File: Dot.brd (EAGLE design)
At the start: 25.4 x 31.5 mm, 42 parts, among them IC1 CAT24M010TS, IC2 SI1145, U1 ATMEGA328P-MU-QFN32, U2 TMP102, U3 ISL29125, U4 9DoF IMU, U5 BMP18

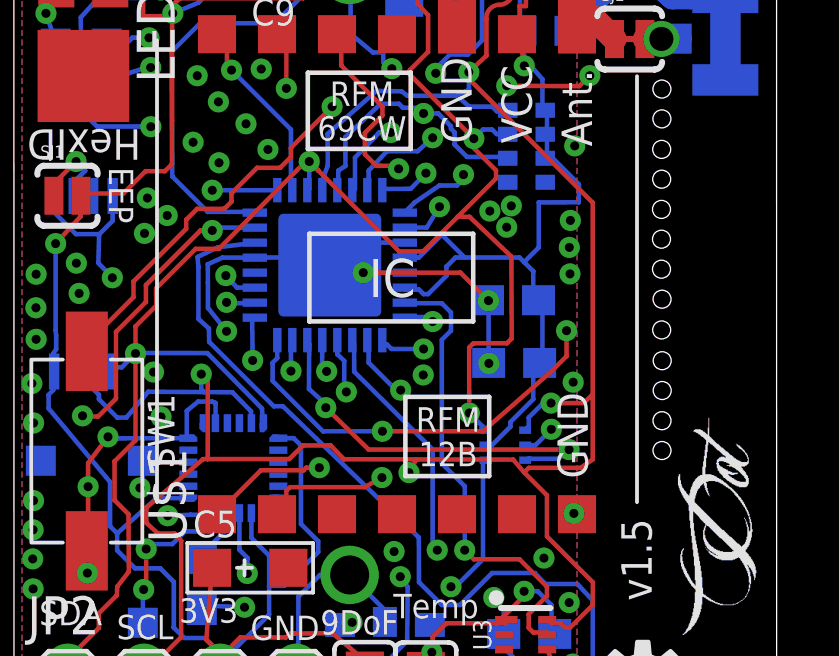
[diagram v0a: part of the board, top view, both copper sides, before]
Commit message: Add pullup to UV, RGB and Temp. Their IRQ share same line
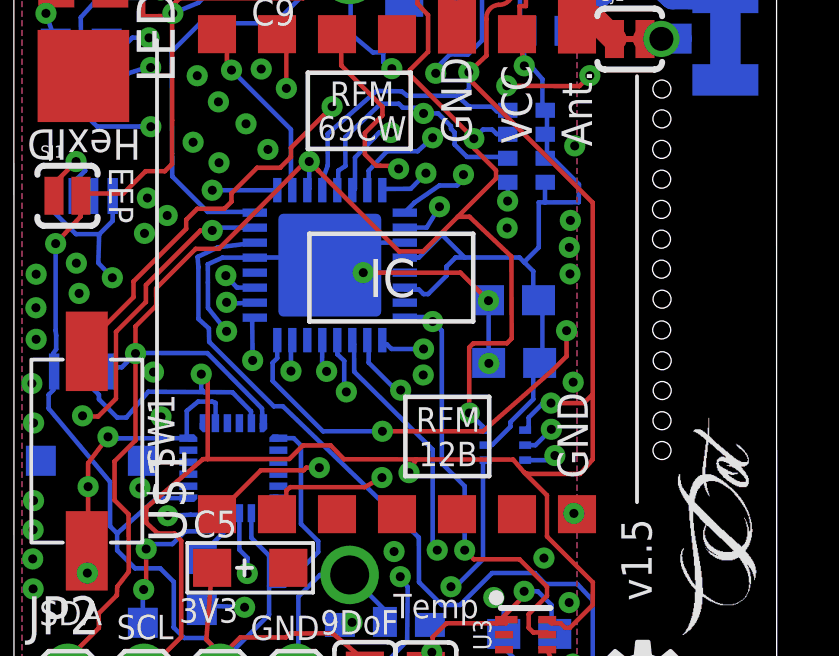
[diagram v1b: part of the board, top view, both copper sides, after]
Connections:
- removed net INT_RGB: U1.7, U3.5
- removed net INT_UV: IC2.4, U1.8
- removed net TEMP_ALERT: U1.14, U2.3
- new net INT_MULTIPLE: IC2.4, R7.1, U1.8, U2.3, U3.5
- net +3V3: now also R7.8
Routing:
- net INT_MULTIPLE: track 0.00 -> 41.3 mm, vias 0 -> 5
- net INT_UV: track 17.1 -> 0.00 mm, vias 2 -> 0
- net INT_RGB: track 15.7 -> 0.00 mm, vias 1 -> 0
- net TEMP_ALERT: track 12.8 -> 0.00 mm, vias 2 -> 0
- net +3V3: track 136.6 -> 137.3 mm
- net GND: vias 53 -> 51

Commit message: ? Checkpoint
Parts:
- added Y1: (no value), SparkFun-Clocks:RESONATOR-SMD-3.2X1.3
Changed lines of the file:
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@@
 <layers>
 <layer number="1" name="Top" color="4" fill="1" visible="yes" active="yes"/>
-<layer number="2" name="Route2" color="1" fill="3" visible="yes" active="yes"/>
+<layer number="2" name="Route2" color="1" fill="3" visible="no" active="yes"/>
 <layer number="3" name="Route3" color="4" fill="3" visible="no" active="no"/>
 <layer number="14" name="Route14" color="1" fill="6" visible="no" active="no"/>
-<layer number="15" name="Route15" color="4" fill="6" visible="yes" active="yes"/>
+<layer number="15" name="Route15" color="4" fill="6" visible="no" active="yes"/>
 <layer number="16" name="Bottom" color="1" fill="1" visible="yes" active="yes"/>
 <layer number="17" name="Pads" color="2" fill="1" visible="yes" active="yes"/>
@@
 <layer number="19" name="Unrouted" color="6" fill="1" visible="yes" active="yes"/>
 <layer number="20" name="Dimension" color="15" fill="1" visible="yes" active="yes"/>
-<layer number="21" name="tPlace" color="7" fill="1" visible="yes" active="yes"/>
-<layer number="22" name="bPlace" color="7" fill="1" visible="yes" active="yes"/>
-<layer number="23" name="tOrigins" color="15" fill="1" visible="yes" active="yes"/>
+<layer number="21" name="tPlace" color="7" fill="1" visible="no" active="yes"/>
+<layer number="22" name="bPlace" color="7" fill="1" visible="no" active="yes"/>
+<layer number="23" name="tOrigins" color="15" fill="1" visible="no" active="yes"/>
 <layer number="24" name="bOrigins" color="15" fill="1" visible="yes" active="yes"/>
 <layer number="25" name="tNames" color="7" fill="1" visible="no" active="yes"/>
@@
 <element name="C7" library="resistor" package="C0603" value="0.1uF" x="16.446503125" y="27.07838125" rot="MR90"/>
 <element name="SJ6" library="SparkFun" package="SJ_2S-NOTRACE" value="SOLDERJUMPERNC2" x="14.466696875" y="28.2892" rot="R90"/>
+<element name="Y1" library="SparkFun-Clocks" package="RESONATOR-SMD-3.2X1.3" value="" x="34.544" y="19.939" rot="MR90"/>
 </elements>
 <signals>

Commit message: Add chrystal oscillator, moved C2 and C3
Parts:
- moved Y1 19.0 mm to (16.0, 15.9)
- moved C3 0.89 mm to (17.8, 15.8), turned to 90 degrees
- moved C2 0.18 mm to (17.0, 13.2)
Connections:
- new net N$6: U1.7, Y1.3
- new net N$8: U1.8, Y1.1
- net GND: now also Y1.2
- net INT_MULTIPLE: now also U1.14; no longer U1.8
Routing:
- net INT_MULTIPLE: track 41.3 -> 48.9 mm, vias 5 -> 6
- net GND: track 133.4 -> 128.1 mm, vias 51 -> 47
- net +3V3: track 137.3 -> 133.1 mm, vias 8 -> 10
- net SDA: track 80.1 -> 84.3 mm
- net N$6: track 0.00 -> 2.65 mm
- net N$8: track 0.00 -> 1.61 mm
- net RSDI: track 15.4 -> 16.2 mm

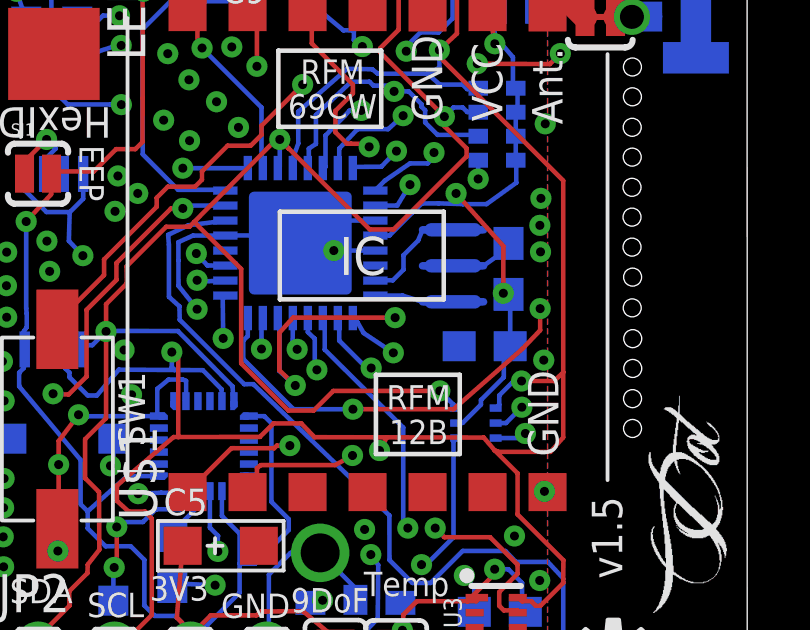
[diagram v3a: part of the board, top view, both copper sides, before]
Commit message: Move chrystal and C2 down to balance osc l-r length
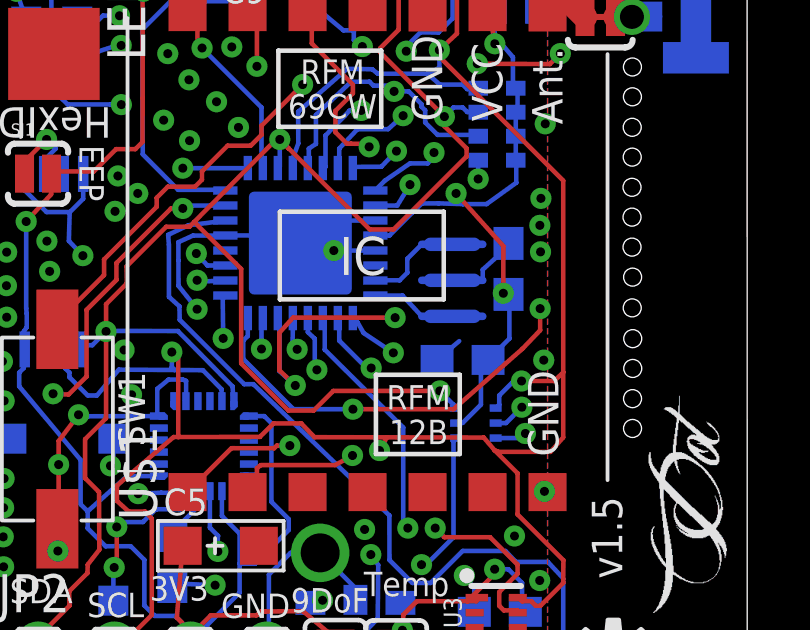
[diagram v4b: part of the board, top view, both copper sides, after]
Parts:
- moved C2 0.87 mm to (16.3, 12.8)
- moved Y1 0.48 mm to (16.0, 15.4)
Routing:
- net GND: track 128.1 -> 129.3 mm
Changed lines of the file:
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@@
 <element name="C8" library="resistor" package="C0603" value="0.1uF" x="6.6193625" y="6.08723125" rot="MR270"/>
 <element name="C1" library="resistor" package="C0603" value="0.1uF" x="18.07685625" y="24.494390625" rot="MR180"/>
-<element name="C2" library="resistor" package="C0603" value="0.1uF" x="17.032075" y="13.246590625" rot="MR0"/>
+<element name="C2" library="resistor" package="C0603" value="0.1uF" x="16.295475" y="12.789390625" rot="MR0"/>
 <element name="C3" library="resistor" package="C0603" value="0.1uF" x="17.826428125" y="15.822665625" rot="MR90"/>
 <element name="C4" library="resistor" package="C0603" value="0.1uF" x="17.5350375" y="4.39166875" rot="MR0"/>
@@
 <element name="C7" library="resistor" package="C0603" value="0.1uF" x="16.446503125" y="27.07838125" rot="MR90"/>
 <element name="SJ6" library="SparkFun" package="SJ_2S-NOTRACE" value="SOLDERJUMPERNC2" x="14.466696875" y="28.2892" rot="R90"/>
-<element name="Y1" library="SparkFun-Clocks" package="RESONATOR-SMD-3.2X1.3" value="" x="15.9766" y="15.9258" rot="MR90"/>
+<element name="Y1" library="SparkFun-Clocks" package="RESONATOR-SMD-3.2X1.3" value="" x="15.9512" y="15.4432" rot="MR90"/>
 </elements>
 <signals>
@@
 <wire x1="4.100575" y1="11.349990625" x2="4.095496875" y2="11.349990625" width="0.1524" layer="15"/>
 <wire x1="4.095496875" y1="11.349990625" x2="3.493515625" y2="10.961371875" width="0.1524" layer="15"/>
-<wire x1="16.182075" y1="13.246590625" x2="16.182075" y2="13.41629375" width="0.1524" layer="16"/>
+<wire x1="15.445475" y1="12.789390625" x2="16.182075" y2="13.41629375" width="0.1524" layer="16"/>
 <wire x1="16.1884375" y1="13.40993125" x2="16.1884375" y2="11.243309375" width="0.1524" layer="15"/>
 <wire x1="16.1884375" y1="11.243309375" x2="19.023078125" y2="8.40866875" width="0.1524" layer="15"/>
@@
 <contactref element="Y1" pad="2"/>
 <wire x1="17.826428125" y1="16.672665625" x2="17.877228125" y2="16.556428125" width="0.1524" layer="16"/>
-<wire x1="17.877228125" y1="16.556428125" x2="16.9926" y2="15.9258" width="0.1524" layer="16"/>
 <wire x1="16.1884375" y1="13.40993125" x2="16.182075" y2="13.41629375" width="0" layer="19" extent="15-16"/>
+<wire x1="17.877228125" y1="16.556428125" x2="17.801028125" y2="16.556428125" width="0.1524" layer="16"/>
+<wire x1="17.801028125" y1="16.556428125" x2="16.9672" y2="15.7988" width="0.1524" layer="16"/>
+<wire x1="16.9672" y1="15.7988" x2="16.9672" y2="15.4432" width="0.1524" layer="16"/>
 </signal>
 <signal name="SDA">
@@
 <wire x1="16.29765625" y1="10.689590625" x2="16.14525625" y2="10.689590625" width="0.1524" layer="16"/>
 <wire x1="16.90725625" y1="11.299190625" x2="16.29765625" y2="10.689590625" width="0.1524" layer="16"/>
-<wire x1="16.90725625" y1="11.451590625" x2="16.90725625" y2="11.299190625" width="0.1524" layer="16"/>
-<wire x1="17.66925625" y1="12.213590625" x2="16.90725625" y2="11.451590625" width="0.1524" layer="16"/>
-<wire x1="17.82165625" y1="13.280390625" x2="17.66925625" y2="13.127990625" width="0.1524" layer="16"/>
 <wire x1="16.14525625" y1="10.689590625" x2="16.07855625" y2="10.683909375" width="0.1524" layer="16"/>
-<wire x1="17.82165625" y1="13.280390625" x2="17.882075" y2="13.246590625" width="0.1524" layer="16"/>
 <wire x1="13.85925625" y1="16.937990625" x2="13.40205625" y2="16.937990625" width="0.1524" layer="16"/>
 <wire x1="14.62125625" y1="17.699990625" x2="13.85925625" y2="16.937990625" width="0.1524" layer="16"/>
@@
 <wire x1="17.12685625" y1="23.571309375" x2="17.3695375" y2="23.328628125" width="0.1524" layer="2"/>
 <contactref element="R7" pad="8"/>
-<wire x1="17.882075" y1="13.246590625" x2="17.882075" y2="14.96781875" width="0.1524" layer="16"/>
 <wire x1="17.882075" y1="14.96781875" x2="17.826428125" y2="14.972665625" width="0.1524" layer="16"/>
-<wire x1="17.66925625" y1="12.213590625" x2="17.66925625" y2="13.211571875" width="0.1524" layer="16"/>
-<wire x1="17.66925625" y1="13.211571875" x2="17.882075" y2="13.246590625" width="0.1524" layer="16"/>
 <wire x1="14.62125625" y1="17.699990625" x2="14.939009375" y2="18.004790625" width="0.1524" layer="16"/>
 <wire x1="14.939009375" y1="18.004790625" x2="15.494" y2="18.0086" width="0.1524" layer="16"/>
@@
 <via x="16.0782" y="18.3388" extent="1-16" drill="0.3"/>
 <wire x1="16.0782" y1="18.3388" x2="16.3068" y2="17.9832" width="0.1524" layer="16"/>
+<wire x1="17.882075" y1="14.96781875" x2="17.8562" y2="14.96781875" width="0.1524" layer="16"/>
+<wire x1="17.8562" y1="14.96781875" x2="17.8562" y2="13.500115625" width="0.1524" layer="16"/>
+<wire x1="17.8562" y1="13.500115625" x2="17.145475" y2="12.789390625" width="0.1524" layer="16"/>
+<wire x1="16.90725625" y1="11.299190625" x2="16.90725625" y2="12.551171875" width="0.1524" layer="16"/>
+<wire x1="16.90725625" y1="12.551171875" x2="17.145475" y2="12.789390625" width="0.1524" layer="16"/>
 <wire x1="13.38685625" y1="16.934390625" x2="13.38685625" y2="15.934390625" width="0" layer="19" extent="16-16"/>
 </signal>
@@
 <contactref element="U1" pad="7"/>
 <contactref element="Y1" pad="3"/>
-<wire x1="14.9606" y1="17.1258" x2="14.8144" y2="16.7702" width="0.1524" layer="16"/>
-<wire x1="14.8144" y1="16.7702" x2="14.3256" y2="16.2814" width="0.1524" layer="16"/>
-<wire x1="14.3256" y1="16.2814" x2="14.3256" y2="15.7988" width="0.1524" layer="16"/>
-<wire x1="14.3256" y1="15.7988" x2="13.97" y2="15.4432" width="0.1524" layer="16"/>
-<wire x1="13.97" y1="15.4432" x2="13.395665625" y2="15.4432" width="0.1524" layer="16"/>
+<wire x1="14.1986" y1="15.4432" x2="13.395665625" y2="15.4432" width="0.1524" layer="16"/>
 <wire x1="13.395665625" y1="15.4432" x2="13.38685625" y2="15.434390625" width="0.1524" layer="16"/>
+<wire x1="14.9352" y1="16.6432" x2="14.4526" y2="16.1606" width="0.1524" layer="16"/>
+<wire x1="14.4526" y1="16.1606" x2="14.4526" y2="15.6972" width="0.1524" layer="16"/>
+<wire x1="14.4526" y1="15.6972" x2="14.1986" y2="15.4432" width="0.1524" layer="16"/>
 </signal>
 <signal name="N$8">
@@
 <contactref element="Y1" pad="1"/>
 <wire x1="13.38685625" y1="14.934390625" x2="14.294809375" y2="14.934390625" width="0.1524" layer="16"/>
-<wire x1="14.294809375" y1="14.934390625" x2="14.9606" y2="14.7258" width="0.1524" layer="16"/>
+<wire x1="14.294809375" y1="14.934390625" x2="14.9352" y2="14.2432" width="0.1524" layer="16"/>
 </signal>
 </signals>
